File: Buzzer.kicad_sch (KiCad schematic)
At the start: 57 parts, among them J1 AudioJack2_Ground, J2 AVR-ISP-6, J3 Screw_Terminal_01x07, J4 Screw_Terminal_01x02, J5 Screw_Terminal_01x02, J6 Screw_Terminal_01x02, J7 Screw_Terminal_01x02, J8 USB-C-Board, Q1 BC547, Q2 BC547, Q3 BC547, Q4 BC547, Q5 BC547, SW1 SW_Reset, SW2 SW_Next, SW3 SW_New, U1 ATmega328-P, U2 HDSP-7401, Y1 16 (or 20) MHz

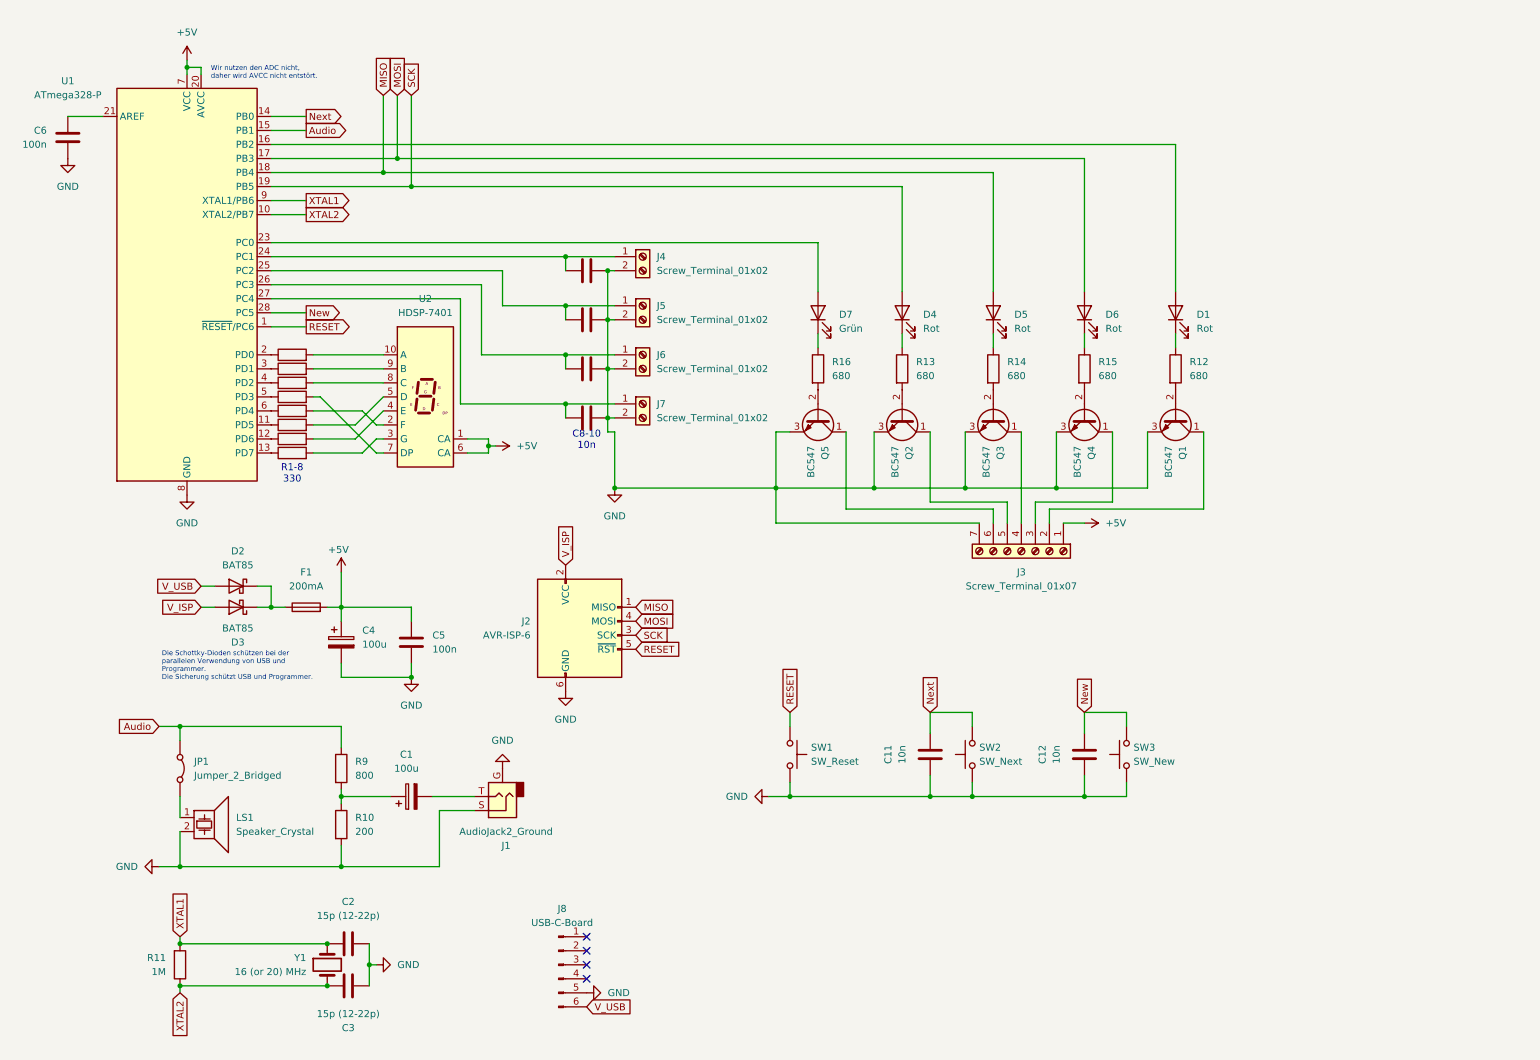
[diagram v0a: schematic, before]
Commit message: Add revision 2 circuit, pcb and documentation.
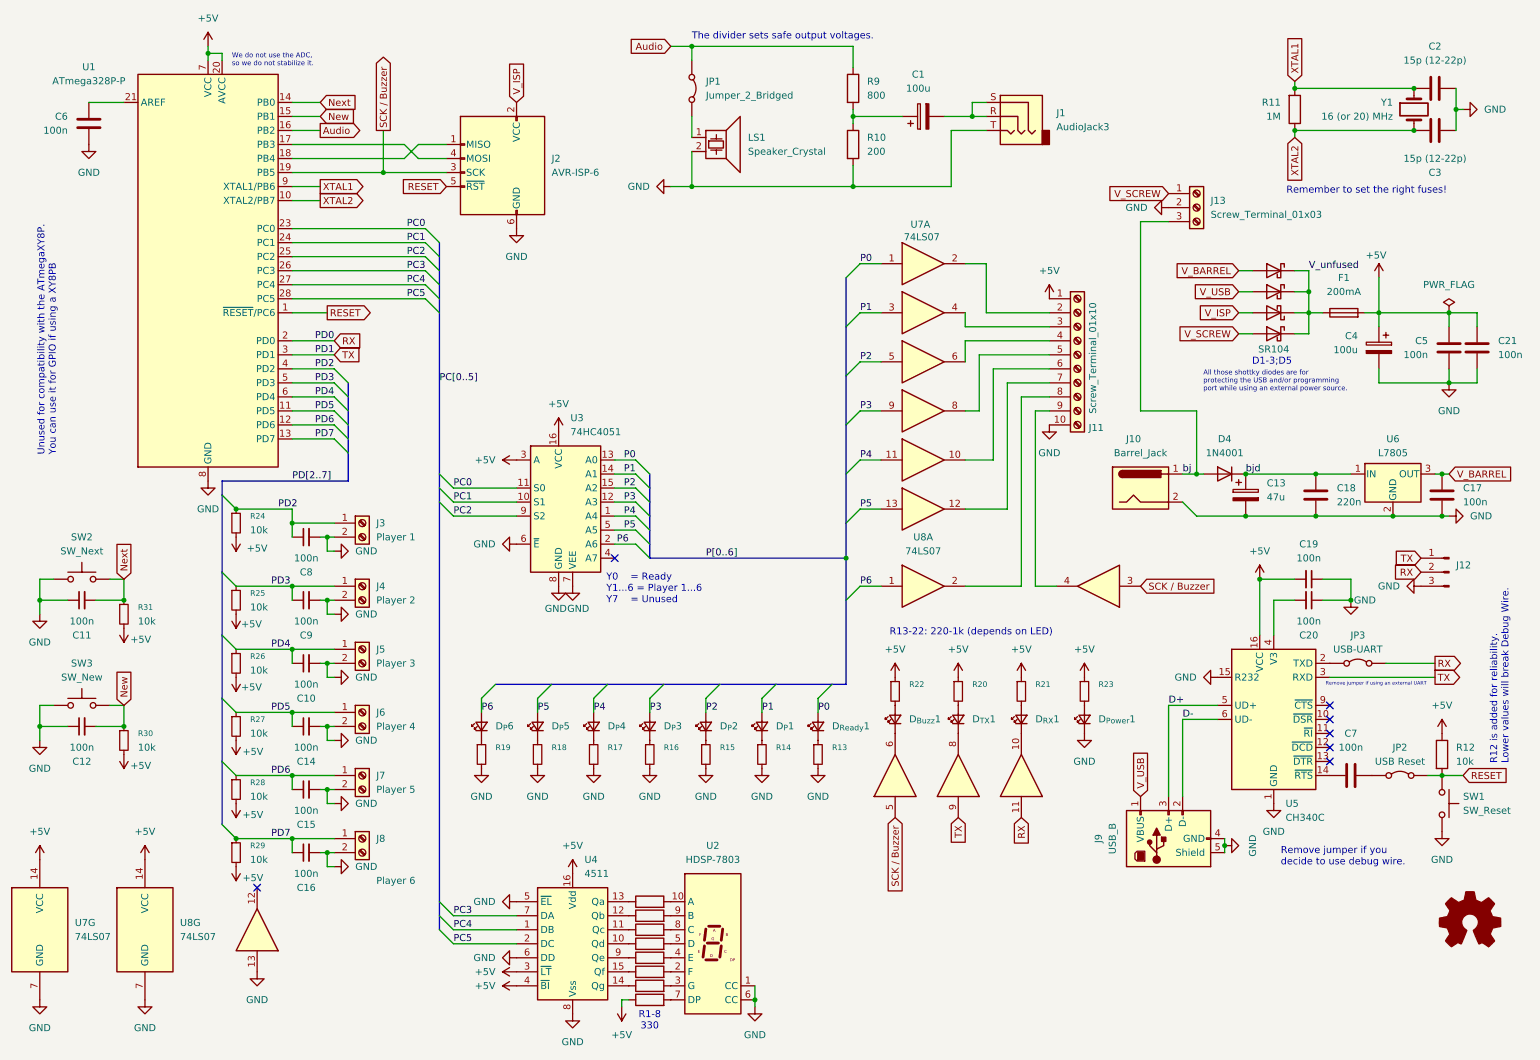
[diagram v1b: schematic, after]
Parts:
- removed C10, C11, C12, C8, C9: 10n, Capacitor_THT:C_Disc_D3.0mm_W1.6mm_P2.50mm, symbol Device:C
- removed D1, D4, D5, D6: Rot, LED_THT:LED_Rectangular_W3.9mm_H1.8mm, symbol Device:LED
- removed D7: Grün, LED_THT:LED_Rectangular_W3.9mm_H1.8mm, symbol Device:LED
- removed J1: AudioJack2_Ground, Connector_Audio:Jack_3.5mm_CUI_SJ1-3523N_Horizontal, symbol Connector_Audio:AudioJack2_Ground
- removed J3: Screw_Terminal_01x07, TerminalBlock_Phoenix:TerminalBlock_Phoenix_MPT-0,5-7-2.54_1x07_P2.54mm_Horizontal, symbol Connector:Screw_Terminal_01x07
- removed J8: USB-C-Board, Connector_PinHeader_2.54mm:PinHeader_1x06_P2.54mm_Horizontal, symbol Connector:Conn_01x06_Pin
- removed Q1, Q2, Q3, Q4, Q5: BC547, Package_TO_SOT_THT:TO-92_Inline_Wide, symbol Transistor_BJT:BC547
- removed R13, R14, R15, R16: 680, Resistor_THT:R_Axial_DIN0204_L3.6mm_D1.6mm_P5.08mm_Horizontal, symbol Device:R
- removed U1: ATmega328-P, Package_DIP:DIP-28_W7.62mm, symbol MCU_Microchip_ATmega:ATmega328-P
- removed U2: HDSP-7401, Display_7Segment:D1X8K, symbol Display_Character:HDSP-7401
- added C10, C11, C12, C14, C15, C16, C19, C20, C8, C9: 100n, Capacitor_THT:C_Disc_D5.0mm_W2.5mm_P2.50mm, symbol Device:C_Small
- added C13: 47u, Capacitor_THT:CP_Radial_D8.0mm_P3.50mm, symbol Device:C_Polarized
- added C17, C21: 100n, Capacitor_THT:C_Disc_D5.0mm_W2.5mm_P2.50mm, symbol Device:C
- added C18: 220n, Capacitor_THT:C_Disc_D5.0mm_W2.5mm_P2.50mm, symbol Device:C
- added D1, D5: SR104, Diode_THT:D_DO-41_SOD81_P7.62mm_Horizontal, symbol Device:D_Schottky
- added D4: 1N4001, Diode_THT:D_DO-41_SOD81_P7.62mm_Horizontal, symbol Diode:1N4001
- added D_{Buzz}1, D_{Power}1, D_{P}1, D_{P}2, D_{P}3, D_{P}4, D_{P}5, D_{P}6, D_{RX}1, D_{Ready}1, D_{TX}1: LED_Small, LED_THT:LED_Rectangular_W5.0mm_H2.0mm, symbol Device:LED_Small
- added J1: AudioJack3, Connector_Audio:Jack_3.5mm_Ledino_KB3SPRS_Horizontal, symbol Connector_Audio:AudioJack3
- added J10: Barrel_Jack, Connector_BarrelJack:BarrelJack_Kycon_KLDX-0202-xC_Horizontal, symbol Connector:Barrel_Jack
- added J11: Screw_Terminal_01x10, TerminalBlock_Phoenix:TerminalBlock_Phoenix_MKDS-1,5-10-5.08_1x10_P5.08mm_Horizontal, symbol Connector:Screw_Terminal_01x10
- added J12: Conn_01x03_Pin, Connector_PinHeader_2.54mm:PinHeader_1x03_P2.54mm_Vertical, symbol Connector:Conn_01x03_Pin
- added J13: Screw_Terminal_01x03, TerminalBlock_Phoenix:TerminalBlock_Phoenix_MKDS-1,5-3-5.08_1x03_P5.08mm_Horizontal, symbol Connector:Screw_Terminal_01x03
- added J3: Player 1, TerminalBlock_Phoenix:TerminalBlock_Phoenix_MKDS-1,5-2-5.08_1x02_P5.08mm_Horizontal, symbol Connector:Screw_Terminal_01x02
- added J8: Player 6, TerminalBlock_Phoenix:TerminalBlock_Phoenix_MKDS-1,5-2-5.08_1x02_P5.08mm_Horizontal, symbol Connector:Screw_Terminal_01x02
- added J9: USB_B, Connector_USB:USB_B_OST_USB-B1HSxx_Horizontal, symbol Connector:USB_B
- added JP2: USB Reset, Connector_PinHeader_2.54mm:PinHeader_1x03_P2.54mm_Vertical, symbol Jumper:Jumper_2_Bridged
- added JP3: USB-UART, Connector_PinHeader_2.54mm:PinHeader_1x03_P2.54mm_Vertical, symbol Jumper:Jumper_2_Bridged
- added R13, R14, R15, R16, R17, R18, R19, R20, R21, R22, R23: 220-1k, Resistor_THT:R_Axial_DIN0207_L6.3mm_D2.5mm_P10.16mm_Horizontal, symbol Device:R_Small
- added R24, R29: 10k, Resistor_THT:R_Axial_DIN0207_L6.3mm_D2.5mm_P7.62mm_Horizontal, symbol Device:R_Small
- added R25, R28, R30, R31: 10k, Resistor_THT:R_Axial_DIN0207_L6.3mm_D2.5mm_P10.16mm_Horizontal, symbol Device:R_Small
- added R26, R27: 10k, Resistor_THT:R_Axial_DIN0207_L6.3mm_D2.5mm_P15.24mm_Horizontal, symbol Device:R_Small
- added U1: ATmega328P-P, Package_DIP:DIP-28_W7.62mm_Socket, symbol MCU_Microchip_ATmega:ATmega328P-P
- added U2: HDSP-7803, Display_7Segment:HDSP-7801, symbol Display_Character:HDSP-7803
- added U3: 74HC4051, Package_DIP:DIP-16_W7.62mm_Socket, symbol 74xx:74HC4051
- added U4: 4511, Package_DIP:DIP-16_W7.62mm_Socket, symbol 4xxx_IEEE:4511
- added U5: CH340C, Package_SO:SOIC-16_3.9x9.9mm_P1.27mm, symbol Interface_USB:CH340C
- added U6: L7805, Package_TO_SOT_THT:TO-220-3_Horizontal_TabDown, symbol Regulator_Linear:L7805
- added U7, U8: 74LS07, Package_DIP:DIP-14_W7.62mm_Socket, symbol 74xx:74LS07
- C1, C4: footprint Capacitor_THT:CP_Radial_D10.0mm_P2.50mm -> Capacitor_THT:CP_Radial_D6.3mm_P2.50mm
- C2, C3: footprint Capacitor_THT:C_Disc_D3.0mm_W1.6mm_P2.50mm -> Capacitor_THT:C_Disc_D5.0mm_W2.5mm_P5.00mm
- C5, C6: footprint Capacitor_THT:C_Disc_D3.0mm_W1.6mm_P2.50mm -> Capacitor_THT:C_Disc_D5.0mm_W2.5mm_P2.50mm
- C7: value 10n -> 100n; footprint Capacitor_THT:C_Disc_D3.0mm_W1.6mm_P2.50mm -> Capacitor_THT:C_Disc_D5.0mm_W2.5mm_P2.50mm
- D2: value BAT85 -> SR104; footprint Diode_THT:D_T-1_P5.08mm_Horizontal -> Diode_THT:D_DO-41_SOD81_P7.62mm_Horizontal
- D3: value BAT85 -> SR104; footprint Diode_THT:D_T-1_P5.08mm_Horizontal -> Diode_THT:D_DO-41_SOD81_P12.70mm_Horizontal
- J4: value Screw_Terminal_01x02 -> Player 2; footprint TerminalBlock_Phoenix:TerminalBlock_Phoenix_MPT-0,5-2-2.54_1x02_P2.54mm_Horizontal -> TerminalBlock_Phoenix:TerminalBlock_Phoenix_MKDS-1,5-2-5.08_1x02_P5.08mm_Horizontal
- J5: value Screw_Terminal_01x02 -> Player 3; footprint TerminalBlock_Phoenix:TerminalBlock_Phoenix_MPT-0,5-2-2.54_1x02_P2.54mm_Horizontal -> TerminalBlock_Phoenix:TerminalBlock_Phoenix_MKDS-1,5-2-5.08_1x02_P5.08mm_Horizontal
- J6: value Screw_Terminal_01x02 -> Player 4; footprint TerminalBlock_Phoenix:TerminalBlock_Phoenix_MPT-0,5-2-2.54_1x02_P2.54mm_Horizontal -> TerminalBlock_Phoenix:TerminalBlock_Phoenix_MKDS-1,5-2-5.08_1x02_P5.08mm_Horizontal
- J7: value Screw_Terminal_01x02 -> Player 5; footprint TerminalBlock_Phoenix:TerminalBlock_Phoenix_MPT-0,5-2-2.54_1x02_P2.54mm_Horizontal -> TerminalBlock_Phoenix:TerminalBlock_Phoenix_MKDS-1,5-2-5.08_1x02_P5.08mm_Horizontal
- JP1: footprint Connector_PinHeader_2.54mm:PinHeader_1x02_P2.54mm_Vertical -> Connector_PinHeader_2.54mm:PinHeader_1x03_P2.54mm_Vertical
- R1, R10, R11, R2, R3, R4, R5, R6, R7, R8, R9: footprint Resistor_THT:R_Axial_DIN0204_L3.6mm_D1.6mm_P5.08mm_Horizontal -> Resistor_THT:R_Axial_DIN0207_L6.3mm_D2.5mm_P10.16mm_Horizontal
- R12: value 680 -> 10k; footprint Resistor_THT:R_Axial_DIN0204_L3.6mm_D1.6mm_P5.08mm_Horizontal -> Resistor_THT:R_Axial_DIN0207_L6.3mm_D2.5mm_P10.16mm_Horizontal
- Y1: footprint Crystal:Resonator-2Pin_W7.0mm_H2.5mm -> Crystal:Crystal_HC49-U_Vertical
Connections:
- net +5V: now also R12.1, R8.1, C19.2, C21.2, J11.1 (Pin_1), R20.1, R21.1, R22.1, R23.1, R24.2, R25.2, R26.2, R27.2, R28.2, R29.2, R30.2, R31.2, U1.20 (AVCC), U1.7 (VCC), U3.16 (VCC), U3.3 (A), U4.16 (Vdd), U4.3 (~{LT}), U4.4 (~{BI}), U5.16 (VCC), U7.14 (VCC), U8.14 (VCC)
- net Audio: now also U1.16 (PB2)
- net GND: now also C10.2, C11.1, C12.1, C13.2, C14.2, C15.2, C16.2, C17.2, C18.2, C19.1, C20.1, C21.1, C8.2, C9.2, D_{Power}1.1 (K), J1.T, J10.2, J11.10 (Pin_10), J12.3 (Pin_3), J13.2 (Pin_2), J3.2 (Pin_2), J8.2 (Pin_2), J9.4 (GND), J9.5 (Shield), R13.2, R14.2, R15.2, R16.2, R17.2, R18.2, R19.2, U1.22 (GND), U1.8 (GND), U2.1 (CC), U2.6 (CC), U3.6 (~{E}), U3.7 (VEE), U3.8 (GND), U4.5 (~{EL}), U4.6 (DD), U4.8 (Vss), U5.1 (GND), U5.15 (R232), U6.2 (GND), U7.7 (GND), U8.13, U8.7 (GND); no longer C7.2
- net New: now also C12.2, R30.1, U1.15 (PB1)
- net Next: now also C11.2, R31.1, U1.14 (PB0)
- net RESET: now also R12.2, JP2.2 (B), U1.1 (~{RESET}/PC6)
- net V_USB: now also J9.1 (VBUS)
- net XTAL1: now also U1.9 (XTAL1/PB6)
- net XTAL2: now also U1.10 (XTAL2/PB7)
- net at R7.1: now also U4.14 (Qg)
- net at R7.2: now also U2.3 (G)
- net at R6.1: now also U4.15 (Qf)
- net at R1.1: now also U4.13 (Qa)
- net at C6.2: now also U1.21 (AREF)
- net at C7.1: now also U5.14 (~{RTS}); no longer J4.1 (Pin_1)
- net PD4: now reaches J5.1 (Pin_1)
- net PD4: now also C10.1, R26.1, U1.6 (PD4)
- net PD5: now reaches J6.1 (Pin_1)
- net PD5: now also C14.1, R27.1, U1.11 (PD5)
- net PD6: now reaches J7.1 (Pin_1)
- net PD6: now also C15.1, R28.1, U1.12 (PD6)
- net at R2.1: now also U4.12 (Qb)
- net at R3.1: now also U4.11 (Qc)
- net at R4.1: now also U4.10 (Qd)
- net at R5.1: now also U4.9 (Qe)
- net at R4.2: now also U2.5 (D)
- net V_unfused: now reaches D2.1 (K), D3.1 (K), F1.1
- net V_unfused: now also D1.1 (K), D5.1 (K)
- net at C1.2: now also J1.R, J1.S
- net at R3.2: now also U2.8 (C)
- net at R5.2: now also U2.4 (E)
- net at R2.2: now also U2.9 (B)
- net at R1.2: now also U2.10 (A)
- net at R8.2: now also U2.7 (DP)
- net at R6.2: now also U2.2 (F)
- net MISO: no longer names the net of J2.1 (MISO)
- net MISO: now also U1.18 (PB4)
- net MOSI: no longer names the net of J2.4 (MOSI)
- net MOSI: now also U1.17 (PB3)
- net SCK renamed SCK / Buzzer
- net SCK / Buzzer: now also U1.19 (PB5), U8.3, U8.5
- new net: J11.6 (Pin_6), U7.10
- new net: D_{P}5.1 (K), R18.1
- new net: D_{Ready}1.1 (K), R13.1
- new net: D_{Buzz}1.1 (K), U8.6
- new net: D_{Buzz}1.2 (A), R22.2
- new net: J11.2 (Pin_2), U7.2
- new net: C20.2, U5.4 (V3)
- new net: D_{Power}1.2 (A), R23.2
- new net: D_{P}4.1 (K), R17.1
- new net: D_{P}2.1 (K), R15.1
- new net: JP3.1 (A), U5.2 (TXD)
- new net: D_{P}3.1 (K), R16.1
- new net: D_{RX}1.1 (K), U8.10
- new net: J11.3 (Pin_3), U7.4
- new net: J11.4 (Pin_4), U7.6
- new net: J11.5 (Pin_5), U7.8
- new net: J11.7 (Pin_7), U7.12
- new net: J11.8 (Pin_8), U8.2
- new net: J11.9 (Pin_9), U8.4
- new net: D_{P}6.1 (K), R19.1
- new net: D_{TX}1.2 (A), R20.2
- new net: C7.2, JP2.1 (A)
- new net: D_{RX}1.2 (A), R21.2
- new net: D_{P}1.1 (K), R14.1
- new net: D_{TX}1.1 (K), U8.8
- new net D+: J9.3 (D+), U5.5 (UD+)
- new net D-: J9.2 (D-), U5.6 (UD-)
- new net P0: D_{Ready}1.2 (A), U3.13 (A0), U7.1
- new net P1: D_{P}1.2 (A), U3.14 (A1), U7.3
- new net P2: D_{P}2.2 (A), U3.15 (A2), U7.5
- new net P3: D_{P}3.2 (A), U3.12 (A3), U7.9
- new net P4: D_{P}4.2 (A), U3.1 (A4), U7.11
- new net P5: D_{P}5.2 (A), U3.5 (A5), U7.13
- new net P6: D_{P}6.2 (A), U3.2 (A6), U8.1
- new net PC0: U1.23 (PC0), U3.11 (S0)
- new net PC1: U1.24 (PC1), U3.10 (S1)
- new net PC2: U1.25 (PC2), U3.9 (S2)
- new net PC3: U1.26 (PC3), U4.7 (DA)
- new net PC4: U1.27 (PC4), U4.1 (DB)
- new net PC5: U1.28 (PC5), U4.2 (DC)
- new net PD2: C8.1, J3.1 (Pin_1), R24.1, U1.4 (PD2)
- new net PD3: C9.1, J4.1 (Pin_1), R25.1, U1.5 (PD3)
- new net PD7: C16.1, J8.1 (Pin_1), R29.1, U1.13 (PD7)
- new net RX: J12.2 (Pin_2), JP3.2 (B), U1.2 (PD0), U8.11
- new net TX: J12.1 (Pin_1), U1.3 (PD1), U5.3 (RXD), U8.9
- new net V_BARREL: C17.1, D1.2 (A), U6.3 (OUT)
- new net V_SCREW: D5.2 (A), J13.1 (Pin_1)
- new net bj: D4.2 (A), J10.1, J13.3 (Pin_3)
- new net bjd: C13.1, C18.1, D4.1 (K), U6.1 (IN)
- no-connect marks 4 -> 7
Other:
- note added: "All those shottky diodes are for protecting the USB and/or programming port while using an external power source."
- note added: "D1-3;D5"
- note added: "R12 is added for reliability. Lower values will break Debug Wire."
- note added: "R13-22: 220-1k (depends on LED)"
- note added: "Remember to set the right fuses!"
- note added: "Remove jumper if using an external UART"
- note added: "Remove jumper if you decide to use debug wire."
- note added: "The divider sets safe output voltages."
- note added: "Unused for compatibility with the ATmegaXY8P. You can use it for GPIO if using a XY8PB"
- note added: "We do not use the ADC, so we do not stabilize it."
- note added: "Y0 = Ready Y1...6 = Player 1...6 Y7 = Unused"
- note removed: "C8-10 10n"
- note removed: "Die Schottky-Dioden schützen bei der parallelen Verwendung von USB und Programmer. Die Sicherung schützt USB und Programmer."
- note removed: "Wir nutzen den ADC nicht, daher wird AVCC nicht entstört."
- company: (none) -> Port39 e.V.
- title: (none) -> Quiz Buzzer
- moved on the sheet: C1, C2, C3, C4, C5, C6, F1, J2, JP1, LS1, R10, R11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

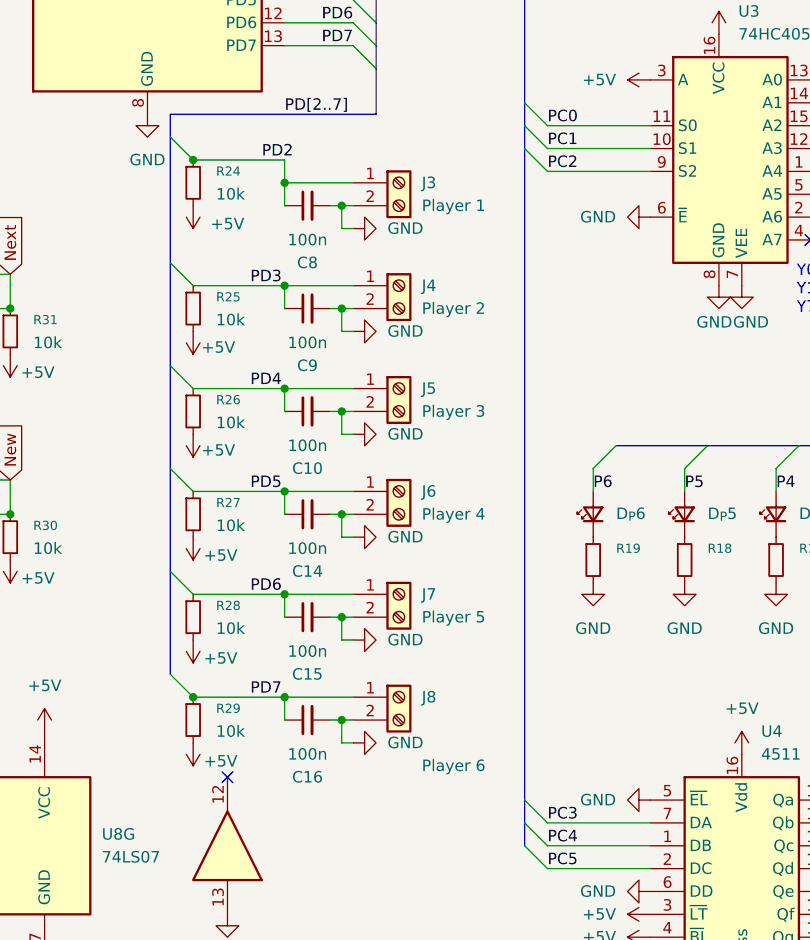
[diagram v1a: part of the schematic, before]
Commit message: Set schematic revisions by variables.
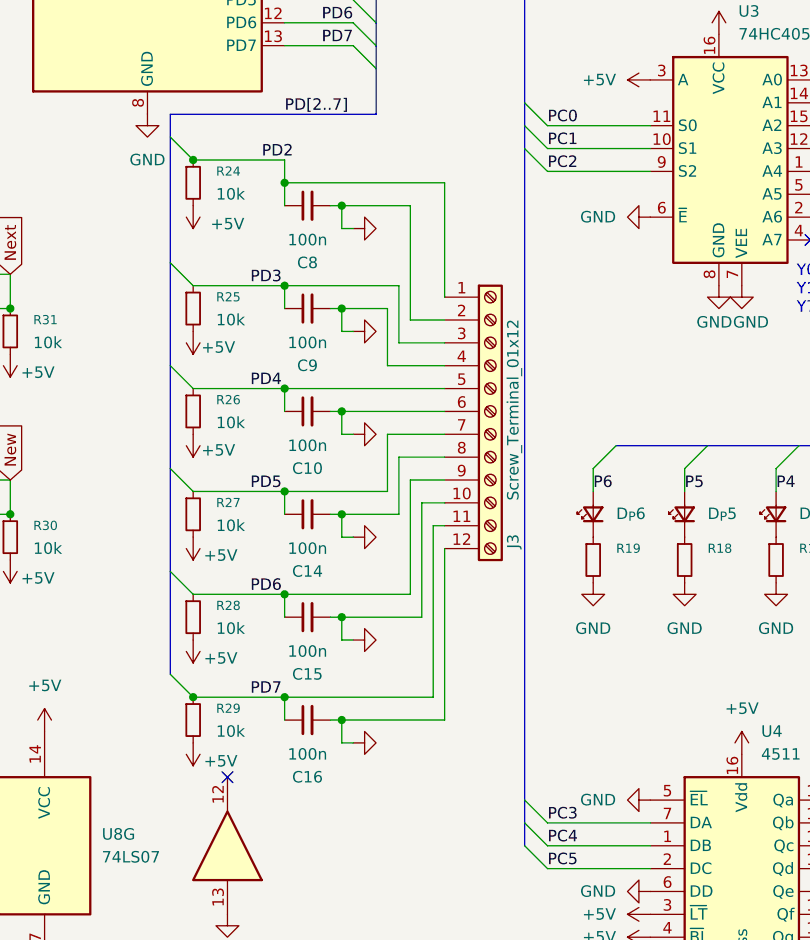
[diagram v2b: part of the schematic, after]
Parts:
- removed J3: Player 1, TerminalBlock_Phoenix:TerminalBlock_Phoenix_MKDS-1,5-2-5.08_1x02_P5.08mm_Horizontal, symbol Connector:Screw_Terminal_01x02
- removed J4: Player 2, TerminalBlock_Phoenix:TerminalBlock_Phoenix_MKDS-1,5-2-5.08_1x02_P5.08mm_Horizontal, symbol Connector:Screw_Terminal_01x02
- removed J5: Player 3, TerminalBlock_Phoenix:TerminalBlock_Phoenix_MKDS-1,5-2-5.08_1x02_P5.08mm_Horizontal, symbol Connector:Screw_Terminal_01x02
- removed J6: Player 4, TerminalBlock_Phoenix:TerminalBlock_Phoenix_MKDS-1,5-2-5.08_1x02_P5.08mm_Horizontal, symbol Connector:Screw_Terminal_01x02
- removed J7: Player 5, TerminalBlock_Phoenix:TerminalBlock_Phoenix_MKDS-1,5-2-5.08_1x02_P5.08mm_Horizontal, symbol Connector:Screw_Terminal_01x02
- removed J8: Player 6, TerminalBlock_Phoenix:TerminalBlock_Phoenix_MKDS-1,5-2-5.08_1x02_P5.08mm_Horizontal, symbol Connector:Screw_Terminal_01x02
- added J3: Screw_Terminal_01x12, TerminalBlock_Phoenix:TerminalBlock_Phoenix_MKDS-1,5-12-5.08_1x12_P5.08mm_Horizontal, symbol Connector:Screw_Terminal_01x12
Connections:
- net GND: now also J3.10 (Pin_10), J3.12 (Pin_12), J3.2 (Pin_2), J3.4 (Pin_4), J3.6 (Pin_6), J3.8 (Pin_8)
- net PD2: now also J3.1 (Pin_1)
- net PD3: now also J3.3 (Pin_3)
- net PD4: now also J3.5 (Pin_5)
- net PD5: now also J3.7 (Pin_7)
- net PD6: now also J3.9 (Pin_9)
- net PD7: now also J3.11 (Pin_11)
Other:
- company: Port39 e.V. -> ${Port39}
- title: Quiz Buzzer -> ${Title}
